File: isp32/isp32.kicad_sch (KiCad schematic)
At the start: 99 parts, among them J1 BAT1, J10 LoRa_ANT, J2 Switching, J3 USB_C_Receptacle_USB2.0, J4 ESP_JTAG, J5 GPS_ANT, J6 F0, J7 F1, J8 Flash_SPI, J9 ANT, M1 Motor_Servo, M2 Motor_Servo, M3 Motor_Servo, M4 Motor_Servo, Q1 BSS138, Q2 BSS138, Q3 IRLML6402, Q4 BSS138, Q5 IRLML6402, Q6 S8050, Q7 S8050, Q8 S8050, SW1 RST, SW2 IO0, U10 BMP280, U11 MPU-9250, U12 CH340C, U2 USBLC6-2SC6, U3 ESP32-WROOM-32U, U4 AMS1117-3.3, U5 MP2303ADN, U7 NEO-XM, U8 AT25SF081-SSHD-X, U9 RFM98W-315S2

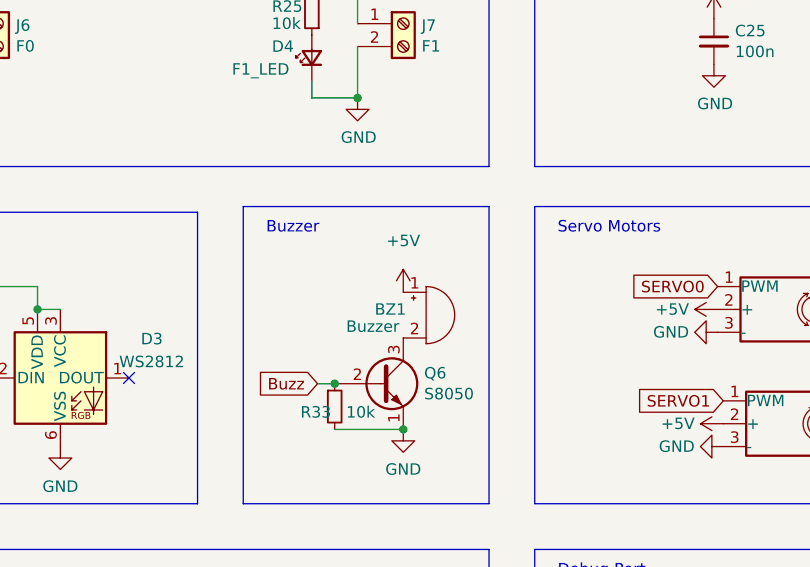
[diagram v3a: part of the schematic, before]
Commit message: Change buzzer type
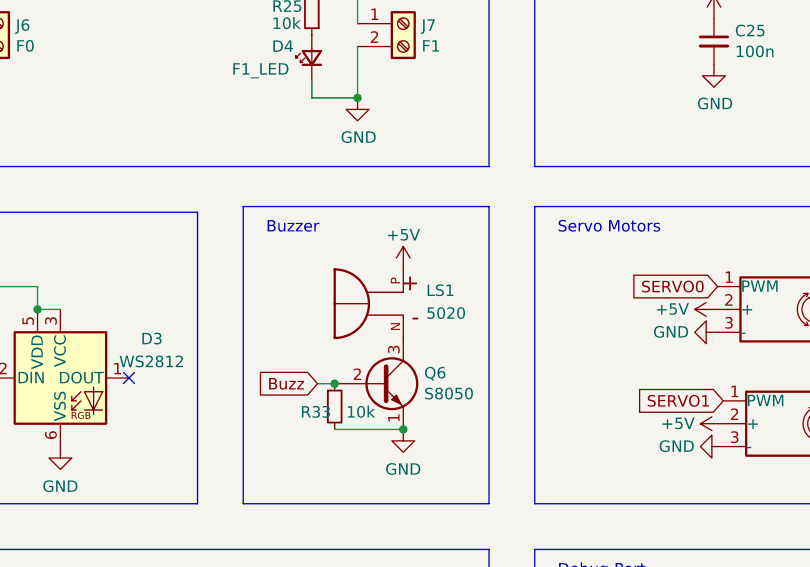
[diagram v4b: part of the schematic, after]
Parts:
- removed BZ1: Buzzer, Buzzer_Beeper:Buzzer_CUI_CPT-9019S-SMT, symbol Device:Buzzer
- added LS1: 5020, Buzzer:XDCR_KSSG33J12-3, symbol KSSG33J12-3:KSSG33J12-3
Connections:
- net +5V: now also LS1.P
- net at Q6.3 (C): now also LS1.N
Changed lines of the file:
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@@
     (pin "6")
+  )
+  (symbol (lib_id "KSSG33J12-3:KSSG33J12-3") (at 353.06 83.185 0) (mirror y) (unit 1)
+    (in_bom yes) (on_board yes) (fields_autoplaced)
+    (property "Reference" "LS1" (id 0) (at 358.14 80.4637 0)
+      (effects (font (size 1.27 1.27)) (justify right))
+    )
+    (property "Value" "5020" (id 1) (at 358.14 83.0037 0)
+      (effects (font (size 1.27 1.27)) (justify right))
+    )
+    (property "Footprint" "Buzzer:XDCR_KSSG33J12-3" (id 2) (at 353.06 83.185 0)
+      (effects (font (size 1.27 1.27)) (justify bottom) hide)
+    )
+    (property "Datasheet" "" (id 3) (at 353.06 83.185 0)
+      (effects (font (size 1.27 1.27)) hide)
+    )
+    (property "PARTREV" "1.4" (id 4) (at 353.06 83.185 0)
+      (effects (font (size 1.27 1.27)) (justify bottom) hide)
+    )
+    (property "MANUFACTURER" "Kingstate" (id 5) (at 353.06 83.185 0)
+      (effects (font (size 1.27 1.27)) (justify bottom) hide)
+    )
+    (property "STANDARD" "Manufacturer recommendations" (id 6) (at 353.06 83.185 0)
+      (effects (font (size 1.27 1.27)) (justify bottom) hide)
+    )
+    (property "MAXIMUM_PACKAGE_HEIGHT" "2.2 mm" (id 7) (at 353.06 83.185 0)
+      (effects (font (size 1.27 1.27)) (justify bottom) hide)
+    )
+    (pin "N")
+    (pin "P")
   )
   (symbol (lib_id "Device:R_Small") (at 434.34 56.515 90) (mirror x) (unit 1)
@@
     (pin "1")
   )
-  (symbol (lib_id "Device:Buzzer") (at 358.14 83.185 0) (unit 1)
-    (in_bom yes) (on_board yes)
-    (property "Reference" "BZ1" (id 0) (at 352.425 82.55 0)
-      (effects (font (size 1.27 1.27)) (justify left))
-    )
-    (property "Value" "Buzzer" (id 1) (at 349.25 84.455 0)
-      (effects (font (size 1.27 1.27)) (justify left))
-    )
-    (property "Footprint" "Buzzer_Beeper:Buzzer_CUI_CPT-9019S-SMT" (id 2) (at 357.505 80.645 90)
-      (effects (font (size 1.27 1.27)) hide)
-    )
-    (property "Datasheet" "~" (id 3) (at 357.505 80.645 90)
-      (effects (font (size 1.27 1.27)) hide)
-    )
-    (pin "1")
-    (pin "2")
-  )
   (symbol (lib_name "+BATT_1") (lib_id "power:+BATT") (at 350.52 29.845 0) (unit 1)
     (in_bom yes) (on_board yes)
@@
     (pin "2")
     (pin "3")
+  )
+  (symbol (lib_name "+5V_5") (lib_id "power:+5V") (at 355.6 78.105 0) (unit 1)
+    (in_bom yes) (on_board yes)
+    (property "Reference" "#PWR0110" (id 0) (at 355.6 81.915 0)
+      (effects (font (size 1.27 1.27)) hide)
+    )
+    (property "Value" "+5V" (id 1) (at 355.6 74.295 0))
+    (property "Footprint" "" (id 2) (at 355.6 78.105 0)
+      (effects (font (size 1.27 1.27)) hide)
+    )
+    (property "Datasheet" "" (id 3) (at 355.6 78.105 0)
+      (effects (font (size 1.27 1.27)) hide)
+    )
+    (pin "1")
   )
   (symbol (lib_id "power:GND") (at 221.615 168.91 0) (unit 1)
@@
     )
     (property "Datasheet" "" (id 3) (at 350.52 59.055 0)
-      (effects (font (size 1.27 1.27)) hide)
-    )
-    (pin "1")
-  )
-  (symbol (lib_name "+5V_5") (lib_id "power:+5V") (at 355.6 80.645 0) (unit 1)
-    (in_bom yes) (on_board yes) (fields_autoplaced)
-    (property "Reference" "#PWR0110" (id 0) (at 355.6 84.455 0)
-      (effects (font (size 1.27 1.27)) hide)
-    )
-    (property "Value" "+5V" (id 1) (at 355.6 74.93 0))
-    (property "Footprint" "" (id 2) (at 355.6 80.645 0)
-      (effects (font (size 1.27 1.27)) hide)
-    )
-    (property "Datasheet" "" (id 3) (at 355.6 80.645 0)
       (effects (font (size 1.27 1.27)) hide)
     )
@@
       (reference "#PWR0109") (unit 1) (value "GND") (footprint "")
     )
-    (path "/ed4dcfb7-f65a-4942-b826-10eb15781e76"
+    (path "/d07b6101-6d0b-4464-a9d4-666e168c3b4b"
       (reference "#PWR0110") (unit 1) (value "+5V") (footprint "")
     )
@@
       (reference "#PWR0205") (unit 1) (value "+3V3") (footprint "")
     )
-    (path "/cd4f641a-ec7d-48d2-8573-0fca19b74d10"
-      (reference "BZ1") (unit 1) (value "Buzzer") (footprint "Buzzer_Beeper:Buzzer_CUI_CPT-9019S-SMT")
-    )
     (path "/0fe6a2f8-00a6-416e-8335-a0098879ae99"
       (reference "C1") (unit 1) (value "100n") (footprint "Capacitor_SMD:C_0603_1608Metric")
@@
       (reference "L2") (unit 1) (value "22u") (footprint "Inductor_SMD:L_0805_2012Metric")
     )
+    (path "/b03a5345-1441-4564-9711-674ed8afcfbf"
+      (reference "LS1") (unit 1) (value "5020") (footprint "Buzzer:XDCR_KSSG33J12-3")
+    )
     (path "/60dbceb4-2f25-469d-b09c-91973de3f8ab"

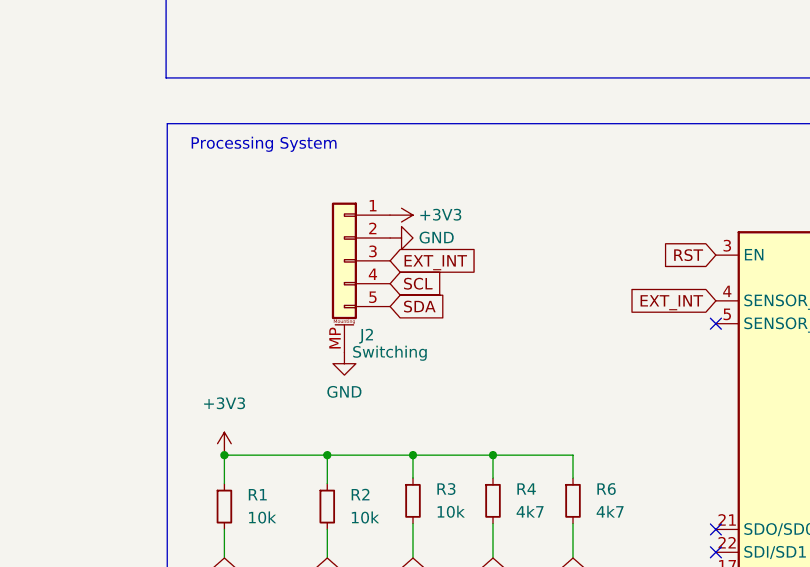
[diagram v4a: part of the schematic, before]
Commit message: Switching port flip
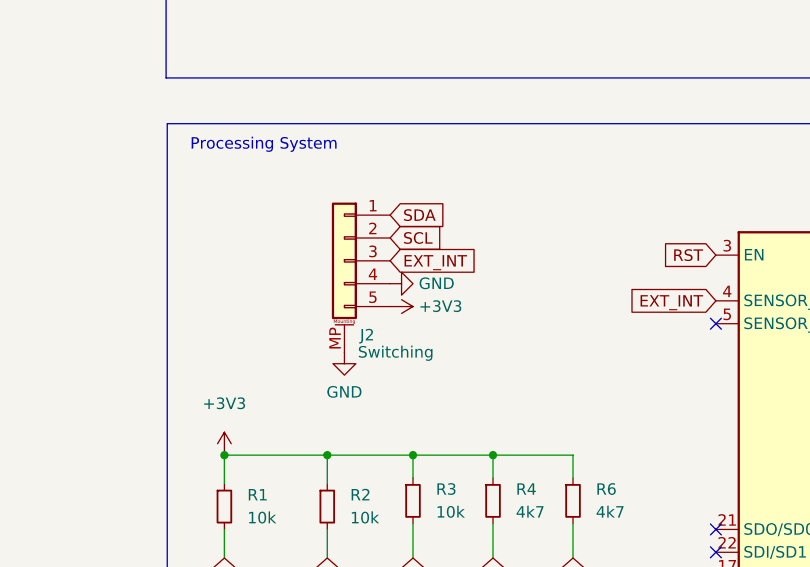
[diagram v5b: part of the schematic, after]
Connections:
- net +3V3: now also J2.5 (Pin_5); no longer J2.1 (Pin_1)
- net GND: now also J2.4 (Pin_4); no longer J2.2 (Pin_2)
- net SCL: now also J2.2 (Pin_2); no longer J2.4 (Pin_4)
- net SDA: now also J2.1 (Pin_1); no longer J2.5 (Pin_5)
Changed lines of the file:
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@@
   (global_label "EXT_INT" (shape input) (at 49.53 124.46 0) (fields_autoplaced)
     (effects (font (size 1.27 1.27)) (justify left))
-    (property "Intersheet References" "${INTERSHEET_REFS}" (id 0) (at 59.1398 124.3806 0)
+    (property "Intersheet References" "${INTERSHEET_REFS}" (id 0) (at 59.1398 124.5394 0)
       (effects (font (size 1.27 1.27)) (justify left) hide)
     )
@@
     )
   )
-  (global_label "SCL" (shape input) (at 49.53 127 0) (fields_autoplaced)
-    (effects (font (size 1.27 1.27)) (justify left))
-    (property "Intersheet References" "${INTERSHEET_REFS}" (id 0) (at 55.4507 126.9206 0)
+  (global_label "SCL" (shape input) (at 49.53 121.92 0) (fields_autoplaced)
+    (effects (font (size 1.27 1.27)) (justify left))
+    (property "Intersheet References" "${INTERSHEET_REFS}" (id 0) (at 55.4507 121.9994 0)
       (effects (font (size 1.27 1.27)) (justify left) hide)
     )
@@
     )
   )
-  (global_label "SDA" (shape input) (at 49.53 129.54 0) (fields_autoplaced)
-    (effects (font (size 1.27 1.27)) (justify left))
-    (property "Intersheet References" "${INTERSHEET_REFS}" (id 0) (at 55.5112 129.4606 0)
+  (global_label "SDA" (shape input) (at 49.53 119.38 0) (fields_autoplaced)
+    (effects (font (size 1.27 1.27)) (justify left))
+    (property "Intersheet References" "${INTERSHEET_REFS}" (id 0) (at 55.5112 119.4594 0)
       (effects (font (size 1.27 1.27)) (justify left) hide)
     )
@@
     (pin "2")
   )
-  (symbol (lib_id "power:GND") (at 49.53 121.92 90) (unit 1)
-    (in_bom yes) (on_board yes) (fields_autoplaced)
-    (property "Reference" "#PWR0186" (id 0) (at 55.88 121.92 0)
-      (effects (font (size 1.27 1.27)) hide)
-    )
-    (property "Value" "GND" (id 1) (at 52.705 121.9199 90)
+  (symbol (lib_id "power:GND") (at 49.53 127 90) (mirror x) (unit 1)
+    (in_bom yes) (on_board yes) (fields_autoplaced)
+    (property "Reference" "#PWR0186" (id 0) (at 55.88 127 0)
+      (effects (font (size 1.27 1.27)) hide)
+    )
+    (property "Value" "GND" (id 1) (at 52.705 127.0001 90)
       (effects (font (size 1.27 1.27)) (justify right))
     )
-    (property "Footprint" "" (id 2) (at 49.53 121.92 0)
-      (effects (font (size 1.27 1.27)) hide)
-    )
-    (property "Datasheet" "" (id 3) (at 49.53 121.92 0)
+    (property "Footprint" "" (id 2) (at 49.53 127 0)
+      (effects (font (size 1.27 1.27)) hide)
+    )
+    (property "Datasheet" "" (id 3) (at 49.53 127 0)
       (effects (font (size 1.27 1.27)) hide)
     )
@@
     (in_bom yes) (on_board yes)
     (property "Reference" "J2" (id 0) (at 46.99 132.715 0))
-    (property "Value" "Switching" (id 1) (at 49.53 134.62 0))
+    (property "Value" "Switching" (id 1) (at 50.165 134.62 0))
     (property "Footprint" "Connector_Molex:Molex_PicoBlade_53261-0571_1x05-1MP_P1.25mm_Horizontal" (id 2) (at 44.45 124.46 0)
       (effects (font (size 1.27 1.27)) hide)
@@
     (pin "1")
   )
-  (symbol (lib_id "power:+3V3") (at 49.53 119.38 270) (unit 1)
-    (in_bom yes) (on_board yes)
-    (property "Reference" "#PWR0187" (id 0) (at 45.72 119.38 0)
-      (effects (font (size 1.27 1.27)) hide)
-    )
-    (property "Value" "+3V3" (id 1) (at 52.705 119.38 90)
-      (effects (font (size 1.27 1.27)) (justify left))
-    )
-    (property "Footprint" "" (id 2) (at 49.53 119.38 0)
-      (effects (font (size 1.27 1.27)) hide)
-    )
-    (property "Datasheet" "" (id 3) (at 49.53 119.38 0)
-      (effects (font (size 1.27 1.27)) hide)
-    )
+  (symbol (lib_id "power:+3V3") (at 49.53 129.54 270) (mirror x) (unit 1)
+    (in_bom yes) (on_board yes)
+    (property "Reference" "#PWR0187" (id 0) (at 45.72 129.54 0)
+      (effects (font (size 1.27 1.27)) hide)
+    )
+    (property "Value" "+3V3" (id 1) (at 52.705 129.54 90)
+      (effects (font (size 1.27 1.27)) (justify left))
+    )
+    (property "Footprint" "" (id 2) (at 49.53 129.54 0)
+      (effects (font (size 1.27 1.27)) hide)
+    )
+    (property "Datasheet" "" (id 3) (at 49.53 129.54 0)
+      (effects (font (size 1.27 1.27)) hide)
+    )

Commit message: Add sd card and pwm controller
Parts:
- removed C20: 100n, Capacitor_SMD:C_0603_1608Metric, symbol Device:C_Small
- removed J8: Flash_SPI, Connector_PinHeader_1.27mm:PinHeader_1x06_P1.27mm_Vertical, symbol Connector_Generic:Conn_01x06
- removed U8: AT25SF081-SSHD-X, Package_SO:SOIC-8_3.9x4.9mm_P1.27mm, symbol Memory_Flash:AT25SF081-SSHD-X
- added C3: 100n, Capacitor_SMD:C_0603_1608Metric, symbol Device:C_Small
- added J12: Micro_SD_Card, Connector_Card:microSD_HC_Molex_47219-2001, symbol Connector:Micro_SD_Card
- added TP3: SWDIO, TestPoint:TestPoint_Pad_D1.0mm, symbol Connector:TestPoint
- added TP4: SWCLK, TestPoint:TestPoint_Pad_D1.0mm, symbol Connector:TestPoint
- added TP5: GND, TestPoint:TestPoint_Pad_D1.0mm, symbol Connector:TestPoint
- added U1: STM32G030J6M6, STM32G030J6:SOIC127P600X175-8N, symbol STM32G030J6M6:STM32G030J6M6
- added U6: 24LC32, Package_SO:SOIC-8_3.9x4.9mm_P1.27mm, symbol Memory_EEPROM:24LC32
- TP1: value TP3v3 -> 3V3
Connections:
- net +3V3: now also C3.1, J12.4 (VDD), U1.2 (VDD/VDDA), U6.8 (VCC)
- net GND: now also C3.2, J12.6 (VSS), J12.9 (SHIELD), TP5.1, U1.3 (VSS/VSSA), U6.1 (A0), U6.2 (A1), U6.3 (A2), U6.4 (GND), U6.7 (WP)
- net IO0: no longer Q2.2 (S), R19.2
- net MISO: now also J12.7 (DAT0)
- net MOSI: now also J12.3 (CMD)
- net SCK: now also J12.5 (CLK)
- net SCL: now also TP4.1, U1.8 (PB5/PB6/PA14-BOOT0/PA15); no longer U7.19 (SCL/SPI_CLK)
- net SDA: now also U1.1 (PB7/PB8/PB9/PC14-OSC32_IN); no longer U7.18 (SDA/~{SPI_CS})
- net SERVO0: now also U1.4 (PA0/PA1/PA2/NRST); no longer U3.27 (IO16)
- net SERVO1: now also U1.5 (PA8/PA11[PA9]/PB0/PB1); no longer U3.26 (IO4)
- net SERVO2: now also U1.7 (PA12[PA10]); no longer U3.29 (IO5)
- net SERVO3: now also TP3.1, U1.6 (PA13); no longer U3.28 (IO17)
- net LORA_RST: now reaches U9.6 (RESET)
- net LORA_RST: now also U3.26 (IO4)
- net RX1: now reaches U7.20 (TXD/SPI_MISO)
- net RX1: now also U3.28 (IO17)
- net TX1: now reaches U7.21 (RXD/SPI_MOSI)
- net TX1: now also U3.27 (IO16)
- net IMU_INT: now reaches U11.12 (INT)
- net IMU_INT: now also U3.5 (SENSOR_VN)
- net FLASH_SS renamed RGB
- net RGB: now also Q2.2 (S), R19.2; no longer R30.2
- new net: U6.5 (SDA), U7.18 (SDA/~{SPI_CS})
- new net: U6.6 (SCL), U7.19 (SCL/SPI_CLK)
- new net SD_SS: J12.2 (DAT3/CD), R30.2, U3.29 (IO5)
- no-connect marks 38 -> 33
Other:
- note added: "PWM Controller"
- moved on the sheet: C22, C23, R17, R30

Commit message: New design with esp32s3
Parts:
- removed C25, C26: 100n, Capacitor_SMD:C_0603_1608Metric, symbol Device:C_Small
- removed Q7, Q8: S8050, Package_TO_SOT_SMD:SOT-23, symbol Transistor_BJT:S8050
- removed R26, R27: 470, Resistor_SMD:R_0603_1608Metric, symbol Device:R_Small
- removed R28, R29, R3: 10k, Resistor_SMD:R_0603_1608Metric, symbol Device:R_Small
- removed U1: STM32G030J6M6, STM32G030J6:SOIC127P600X175-8N, symbol STM32G030J6M6:STM32G030J6M6
- removed U12: CH340C, Package_SO:SOIC-16_3.9x9.9mm_P1.27mm, symbol Interface_USB:CH340C
- removed U3: ESP32-WROOM-32U, RF_Module:ESP32-WROOM-32U, symbol RF_Module:ESP32-WROOM-32U
- added TP6: 3V3, TestPoint:TestPoint_Pad_D1.0mm, symbol Connector:TestPoint
- added TP7: SWDIO, TestPoint:TestPoint_Pad_D1.0mm, symbol Connector:TestPoint
- added TP8: SWCLK, TestPoint:TestPoint_Pad_D1.0mm, symbol Connector:TestPoint
- added TP9: GND, TestPoint:TestPoint_Pad_D1.0mm, symbol Connector:TestPoint
- added U3: STM32F030F4Px, Package_SO:TSSOP-20_4.4x6.5mm_P0.65mm, symbol MCU_ST_STM32F0:STM32F030F4Px
- added U8: ESP32-S3-WROOM-1U, ESP32-S3-WROOM-1U:XCVR_ESP32-S3-WROOM-1U, symbol ESP32-S3-WROOM-1U:ESP32-S3-WROOM-1U
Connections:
- net +3V3: now also TP6.1, U3.16 (VDD), U3.5 (VDDA), U8.2 (3V3)
- net Buzz: now also U8.39 (IO1)
- net D+: now also U8.14 (IO20)
- net D-: now also U8.13 (IO19)
- net EXT_INT: now also U8.9 (IO16)
- net FIRE0: now also U8.24 (IO47)
- net FIRE1: now also U8.25 (IO48)
- net GND: now also TP9.1, U3.1 (BOOT0), U3.15 (VSS), U8.1 (GND), U8.40 (GND), U8.41_1 (GND), U8.41_2 (GND), U8.41_3 (GND), U8.41_4 (GND), U8.41_5 (GND), U8.41_6 (GND), U8.41_7 (GND), U8.41_8 (GND), U8.41_9 (GND)
- net IMU_INT: now also U8.8 (IO15)
- net IMU_SS: now also U8.6 (IO6)
- net IO0: now also U8.27 (IO0)
- net LORA_RST: now also U8.23 (IO21)
- net LORA_SS: now also U8.38 (IO2)
- net MISO: now also U8.30 (IO37)
- net MOSI: now also U8.28 (IO35)
- net RST: now also U3.4 (NRST), U8.3 (EN)
- net RX1: now also U8.10 (IO17)
- net SCK: now also U8.29 (IO36)
- net SCL: now also U3.17 (PA9), U8.12 (IO8); no longer TP4.1
- net SDA: now also U3.18 (PA10), U8.17 (IO9)
- net SD_SS: now also U8.5 (IO5)
- net SERVO0: now also U3.6 (PA0)
- net SERVO1: now also U3.7 (PA1)
- net SERVO2: now also U3.8 (PA2)
- net SERVO3: now also U3.9 (PA3); no longer TP3.1
- net TCK: now also U8.32 (IO39)
- net TDI: now also U8.34 (IO41)
- net TDO: now also U8.33 (IO40)
- net TMS: now also U8.35 (IO42)
- net TX1: now also U8.11 (IO18)
- net UD-: now reaches J3.A7 (D-), J3.B7 (D-), U2.1 (I/O1)
- net UD+: now reaches J3.A6 (D+), J3.B6 (D+), U2.3 (I/O2)
- new net RX: TP8.1, U8.37 (TXD0)
- new net SWCLK: TP4.1, U3.20 (PA14)
- new net SWDIO: TP3.1, U3.19 (PA13)
- new net TX: TP7.1, U8.36 (RXD0)
- no-connect marks 33 -> 38
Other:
- note added: "SD Card"
- note removed: "Flash"
- note removed: "USB To UART"
- moved on the sheet: C3, H1, H2, H3, H4, J12, J4, M1, M2, M3, M4, R30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
